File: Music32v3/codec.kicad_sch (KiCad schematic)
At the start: 29 parts, among them J2 PJ-316A-6A, U3 ES8327

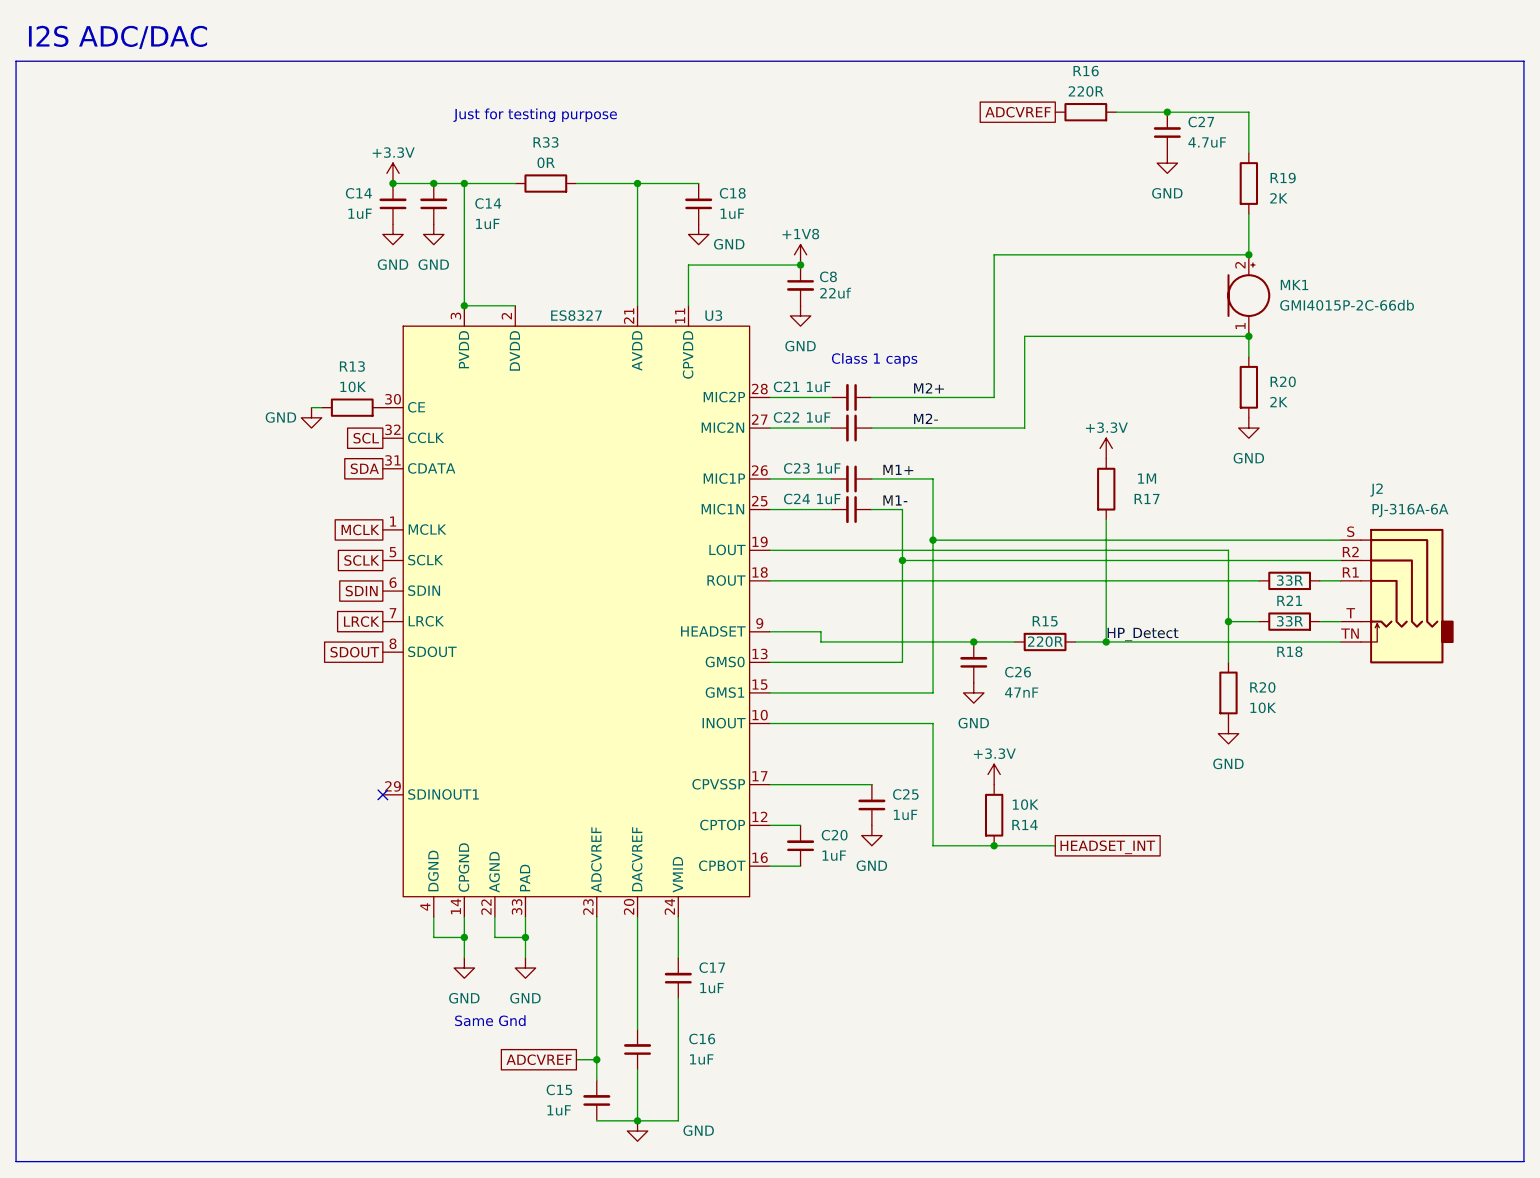
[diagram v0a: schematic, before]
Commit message: PCB outline
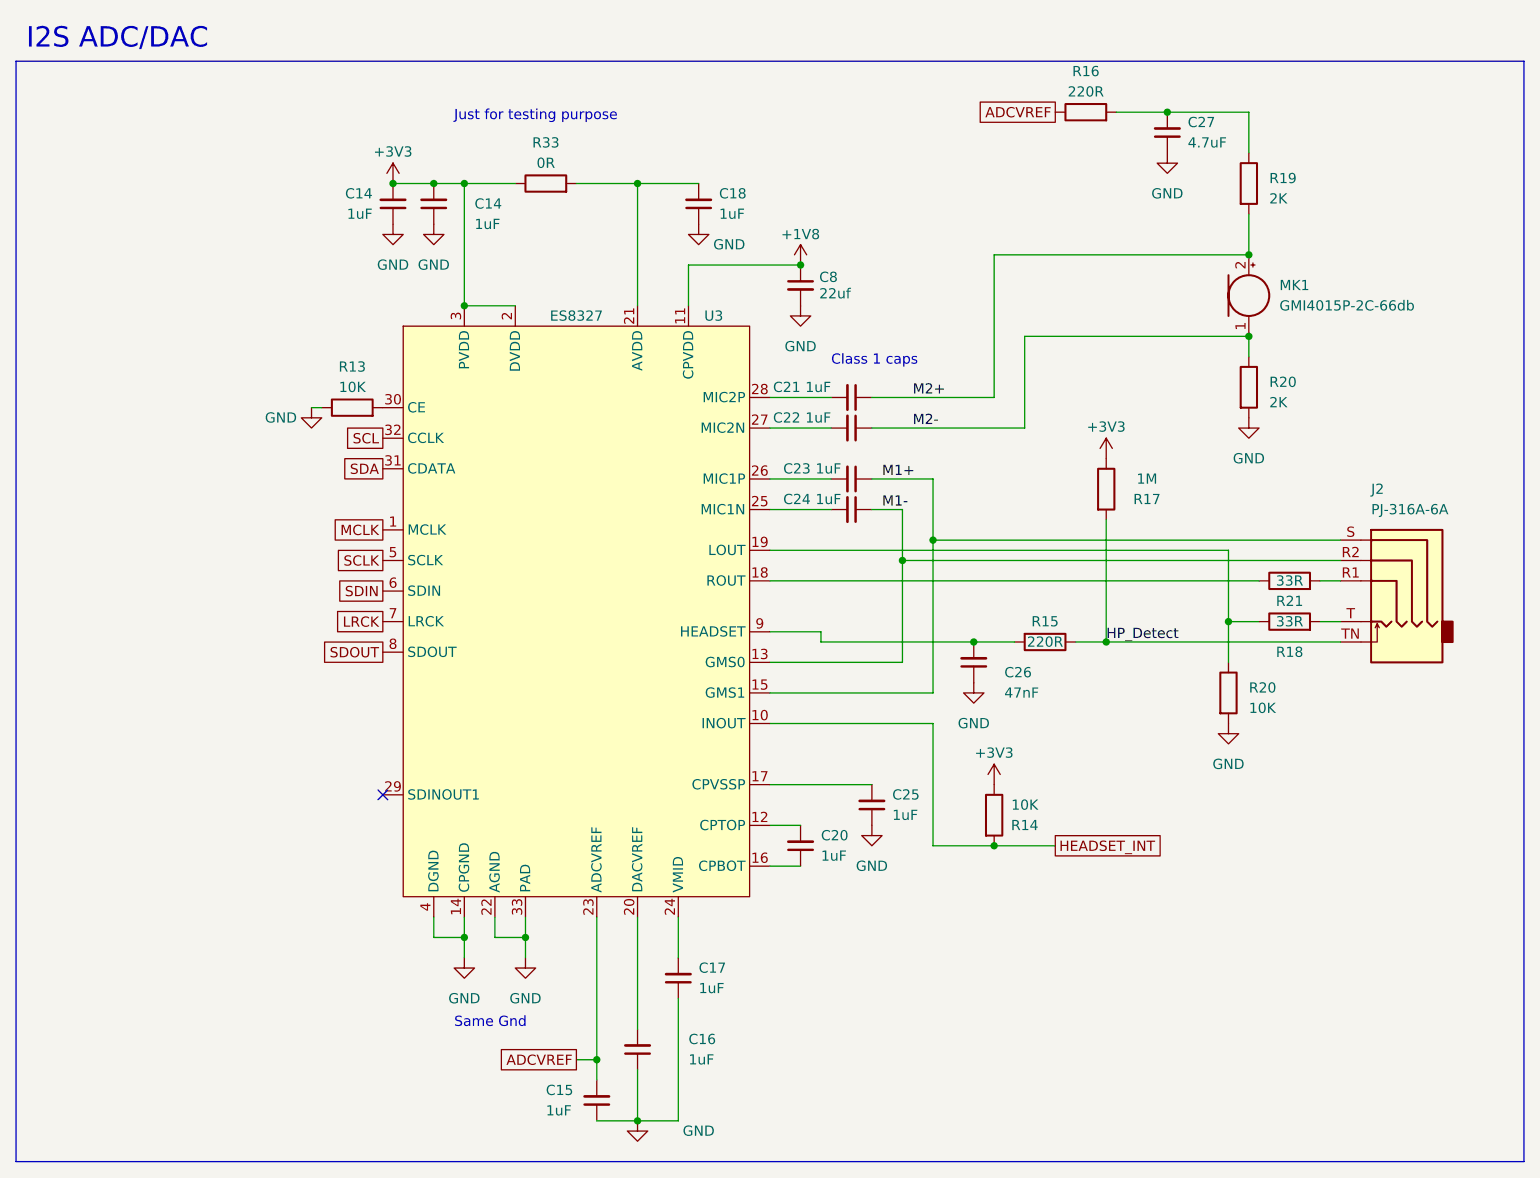
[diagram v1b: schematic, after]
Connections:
- net +3.3V renamed +3V3
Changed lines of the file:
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@@
+    )
+  )
+  (symbol (lib_id "power:+3V3") (at 185.42 73.66 0) (unit 1)
+    (in_bom yes) (on_board yes) (dnp no) (fields_autoplaced)
+    (property "Reference" "#PWR011" (at 185.42 77.47 0)
+      (effects (font (size 1.27 1.27)) hide)
+    )
+    (property "Value" "+3V3" (at 185.42 69.715 0)
+      (effects (font (size 1.27 1.27)))
+    )
+    (property "Footprint" "" (at 185.42 73.66 0)
+      (effects (font (size 1.27 1.27)) hide)
+    )
+    (property "Datasheet" "" (at 185.42 73.66 0)
+      (effects (font (size 1.27 1.27)) hide)
+    )
+    (pin "1")
+    (instances
+      (project "Music32v3"
+        (path "/492e826b-8900-4c12-8604-1c812b2e1995/4998783d-7055-40b0-9979-647930a37834"
+          (reference "#PWR011") (unit 1)
+        )
+        (path "/492e826b-8900-4c12-8604-1c812b2e1995/d3a81cb8-516c-4320-9b3b-4dd6f93f2457"
+          (reference "#PWR092") (unit 1)
+        )
+      )
     )
   )
@@
     )
   )
-  (symbol (lib_id "power:+3.3V") (at 185.42 73.66 0) (unit 1)
-    (in_bom yes) (on_board yes) (dnp no) (fields_autoplaced)
-    (property "Reference" "#PWR041" (at 185.42 77.47 0)
-      (effects (font (size 1.27 1.27)) hide)
-    )
-    (property "Value" "+3.3V" (at 185.42 69.85 0)
-      (effects (font (size 1.27 1.27)))
-    )
-    (property "Footprint" "" (at 185.42 73.66 0)
-      (effects (font (size 1.27 1.27)) hide)
-    )
-    (property "Datasheet" "" (at 185.42 73.66 0)
-      (effects (font (size 1.27 1.27)) hide)
-    )
-    (pin "1")
-    (instances
-      (project "Music_32_V2"
-        (path "/14681cc8-ddd4-43ff-b571-daca84d76d6b/386f7fcb-de3c-43a3-99bd-dcf77f99c217"
-          (reference "#PWR041") (unit 1)
-        )
-      )
-      (project "Audio test board"
-        (path "/20b27d83-997e-4e2f-816d-b30d828687eb"
-          (reference "#PWR?") (unit 1)
-        )
-      )
-      (project "Music32v3"
-        (path "/492e826b-8900-4c12-8604-1c812b2e1995"
-          (reference "#PWR099") (unit 1)
-        )
-        (path "/492e826b-8900-4c12-8604-1c812b2e1995/d3a81cb8-516c-4320-9b3b-4dd6f93f2457"
-          (reference "#PWR092") (unit 1)
-        )
-      )
-      (project "Ipod"
-        (path "/c4cf9ad0-abea-4c32-bb0b-367e5261d002"
-          (reference "#PWR?") (unit 1)
-        )
-        (path "/c4cf9ad0-abea-4c32-bb0b-367e5261d002/5d3aff9d-fc6a-43d3-b155-90242dcdd40f"
-          (reference "#PWR035") (unit 1)
-        )
-      )
-    )
-  )
   (symbol (lib_id "Device:Microphone") (at 203.2 53.34 0) (unit 1)
     (in_bom yes) (on_board yes) (dnp no)
@@
         (path "/c4cf9ad0-abea-4c32-bb0b-367e5261d002/5d3aff9d-fc6a-43d3-b155-90242dcdd40f"
           (reference "R13") (unit 1)
-        )
-      )
-    )
-  )
-  (symbol (lib_id "power:+3.3V") (at 96.52 39.37 0) (mirror y) (unit 1)
-    (in_bom yes) (on_board yes) (dnp no) (fields_autoplaced)
-    (property "Reference" "#PWR029" (at 96.52 43.18 0)
-      (effects (font (size 1.27 1.27)) hide)
-    )
-    (property "Value" "+3.3V" (at 96.52 35.56 0)
-      (effects (font (size 1.27 1.27)))
-    )
-    (property "Footprint" "" (at 96.52 39.37 0)
-      (effects (font (size 1.27 1.27)) hide)
-    )
-    (property "Datasheet" "" (at 96.52 39.37 0)
-      (effects (font (size 1.27 1.27)) hide)
-    )
-    (pin "1")
-    (instances
-      (project "Music_32_V2"
-        (path "/14681cc8-ddd4-43ff-b571-daca84d76d6b/386f7fcb-de3c-43a3-99bd-dcf77f99c217"
-          (reference "#PWR029") (unit 1)
-        )
-      )
-      (project "Audio test board"
-        (path "/20b27d83-997e-4e2f-816d-b30d828687eb"
-          (reference "#PWR?") (unit 1)
-        )
-      )
-      (project "Music32v3"
-        (path "/492e826b-8900-4c12-8604-1c812b2e1995"
-          (reference "#PWR087") (unit 1)
-        )
-        (path "/492e826b-8900-4c12-8604-1c812b2e1995/d3a81cb8-516c-4320-9b3b-4dd6f93f2457"
-          (reference "#PWR080") (unit 1)
-        )
-      )
-      (project "Ipod"
-        (path "/c4cf9ad0-abea-4c32-bb0b-367e5261d002"
-          (reference "#PWR?") (unit 1)
-        )
-        (path "/c4cf9ad0-abea-4c32-bb0b-367e5261d002/5d3aff9d-fc6a-43d3-b155-90242dcdd40f"
-          (reference "#PWR023") (unit 1)
         )
       )
@@
         (path "/c4cf9ad0-abea-4c32-bb0b-367e5261d002/5d3aff9d-fc6a-43d3-b155-90242dcdd40f"
           (reference "#PWR032") (unit 1)
-        )
-      )
-    )
-  )
-  (symbol (lib_id "power:+3.3V") (at 171.45 114.3 0) (unit 1)
-    (in_bom yes) (on_board yes) (dnp no) (fields_autoplaced)
-    (property "Reference" "#PWR040" (at 171.45 118.11 0)
-      (effects (font (size 1.27 1.27)) hide)
-    )
-    (property "Value" "+3.3V" (at 171.45 110.49 0)
-      (effects (font (size 1.27 1.27)))
-    )
-    (property "Footprint" "" (at 171.45 114.3 0)
-      (effects (font (size 1.27 1.27)) hide)
-    )
-    (property "Datasheet" "" (at 171.45 114.3 0)
-      (effects (font (size 1.27 1.27)) hide)
-    )
-    (pin "1")
-    (instances
-      (project "Music_32_V2"
-        (path "/14681cc8-ddd4-43ff-b571-daca84d76d6b/386f7fcb-de3c-43a3-99bd-dcf77f99c217"
-          (reference "#PWR040") (unit 1)
-        )
-      )
-      (project "Audio test board"
-        (path "/20b27d83-997e-4e2f-816d-b30d828687eb"
-          (reference "#PWR?") (unit 1)
-        )
-      )
-      (project "Music32v3"
-        (path "/492e826b-8900-4c12-8604-1c812b2e1995"
-          (reference "#PWR098") (unit 1)
-        )
-        (path "/492e826b-8900-4c12-8604-1c812b2e1995/d3a81cb8-516c-4320-9b3b-4dd6f93f2457"
-          (reference "#PWR091") (unit 1)
-        )
-      )
-      (project "Ipod"
-        (path "/c4cf9ad0-abea-4c32-bb0b-367e5261d002"
-          (reference "#PWR?") (unit 1)
-        )
-        (path "/c4cf9ad0-abea-4c32-bb0b-367e5261d002/5d3aff9d-fc6a-43d3-b155-90242dcdd40f"
-          (reference "#PWR034") (unit 1)
         )
       )
@@
     )
   )
+  (symbol (lib_id "power:+3V3") (at 96.52 39.37 0) (unit 1)
+    (in_bom yes) (on_board yes) (dnp no) (fields_autoplaced)
+    (property "Reference" "#PWR011" (at 96.52 43.18 0)
+      (effects (font (size 1.27 1.27)) hide)
+    )
+    (property "Value" "+3V3" (at 96.52 35.425 0)
+      (effects (font (size 1.27 1.27)))
+    )
+    (property "Footprint" "" (at 96.52 39.37 0)
+      (effects (font (size 1.27 1.27)) hide)
+    )
+    (property "Datasheet" "" (at 96.52 39.37 0)
+      (effects (font (size 1.27 1.27)) hide)
+    )
+    (pin "1")
+    (instances
+      (project "Music32v3"
+        (path "/492e826b-8900-4c12-8604-1c812b2e1995/4998783d-7055-40b0-9979-647930a37834"
+          (reference "#PWR011") (unit 1)
+        )
+        (path "/492e826b-8900-4c12-8604-1c812b2e1995/d3a81cb8-516c-4320-9b3b-4dd6f93f2457"
+          (reference "#PWR080") (unit 1)
+        )
+      )
+    )
+  )
   (symbol (lib_id "power:GND") (at 134.62 44.45 0) (unit 1)
     (in_bom yes) (on_board yes) (dnp no)
@@
         )
       )
+    )
+  )
+  (symbol (lib_id "power:+3V3") (at 171.45 114.3 0) (unit 1)
+    (in_bom yes) (on_board yes) (dnp no) (fields_autoplaced)
+    (property "Reference" "#PWR011" (at 171.45 118.11 0)
+      (effects (font (size 1.27 1.27)) hide)
+    )
+    (property "Value" "+3V3" (at 171.45 110.355 0)
+      (effects (font (size 1.27 1.27)))
+    )
+    (property "Footprint" "" (at 171.45 114.3 0)
+      (effects (font (size 1.27 1.27)) hide)
+    )
+    (property "Datasheet" "" (at 171.45 114.3 0)
+      (effects (font (size 1.27 1.27)) hide)
+    )
+    (pin "1")
+    (instances
+      (project "Music32v3"
+        (path "/492e826b-8900-4c12-8604-1c812b2e1995/4998783d-7055-40b0-9979-647930a37834"
+          (reference "#PWR011") (unit 1)
+        )
+        (path "/492e826b-8900-4c12-8604-1c812b2e1995/d3a81cb8-516c-4320-9b3b-4dd6f93f2457"
+          (reference "#PWR091") (unit 1)
+        )
+      )

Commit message: Board setup
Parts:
- added TP6 (x4): TestPoint, TestPoint:TestPoint_Pad_D1.5mm, symbol Connector:TestPoint
- added TP6 (x2): TestPoint, TestPoint:TestPoint_Pad_D2.0mm, symbol Connector:TestPoint
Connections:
- net HEADSET_INT: now also TP6.1
- net LRCK: now also TP6.1
- net SCLK: now also TP6.1
- net SDIN: now also TP6.1
- net SDOUT: now also TP6.1
- net MCLK renamed MCLK_TXD
- net MCLK_TXD: now also TP6.1
